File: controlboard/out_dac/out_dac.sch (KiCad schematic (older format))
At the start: 16 parts, among them J1 CONN_01X20, U1 PCM5102

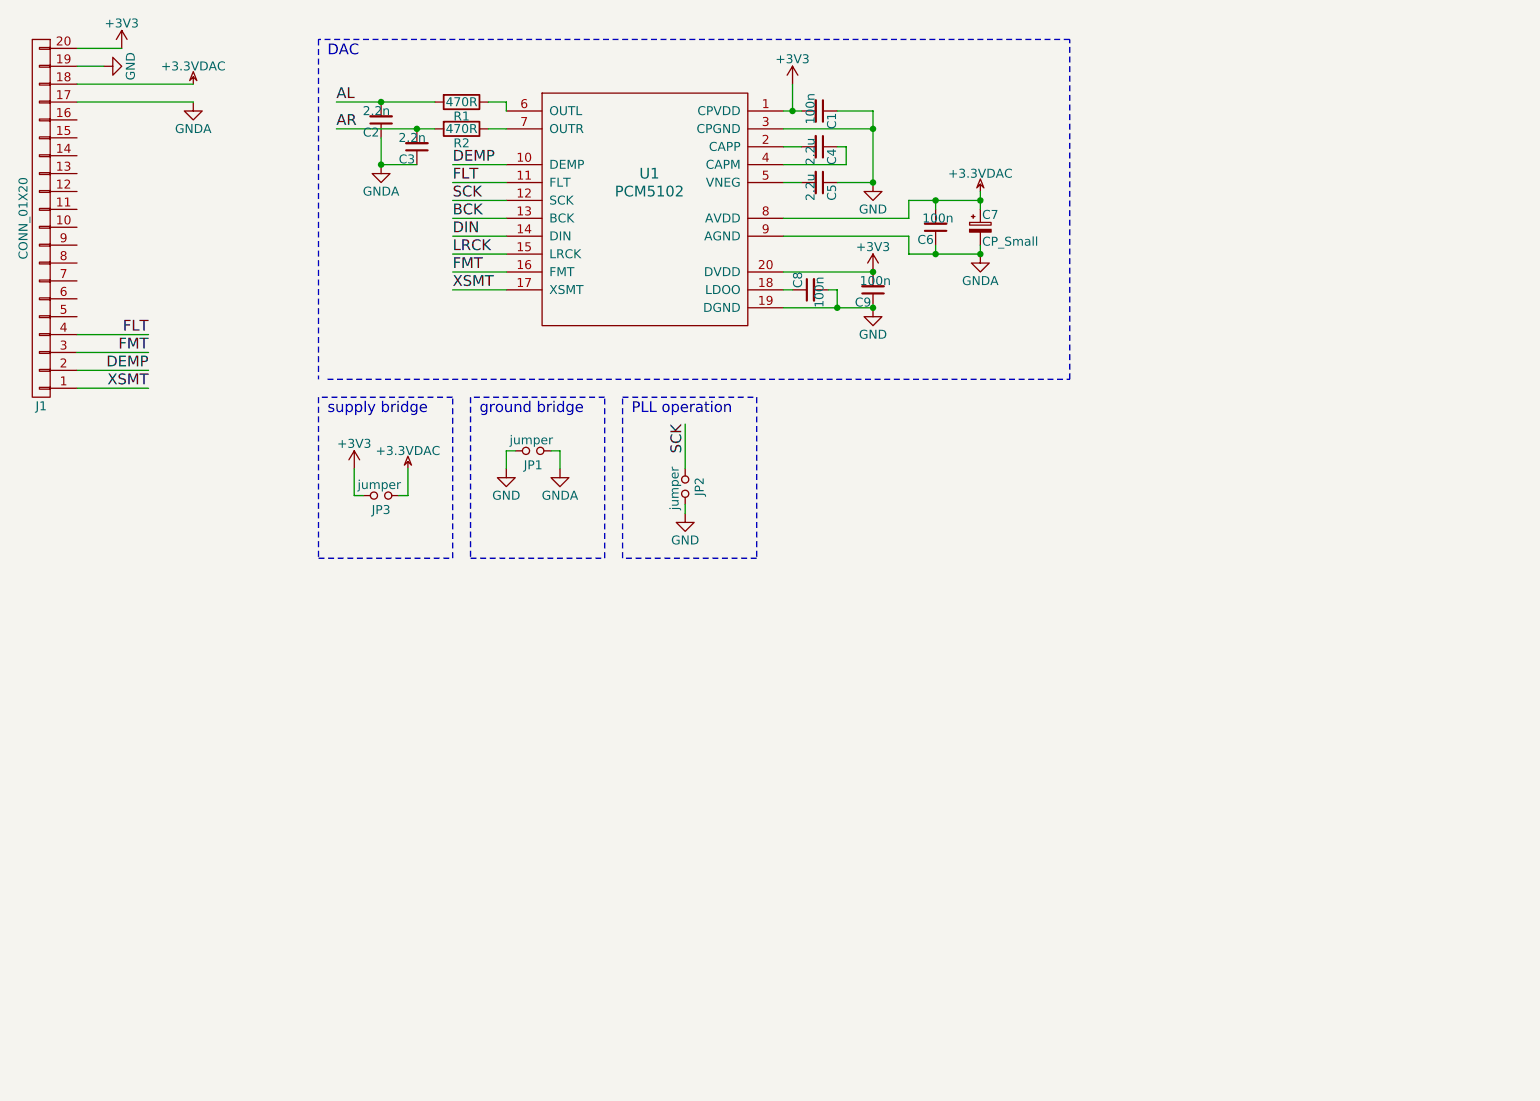
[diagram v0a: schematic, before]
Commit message: add vol control IC
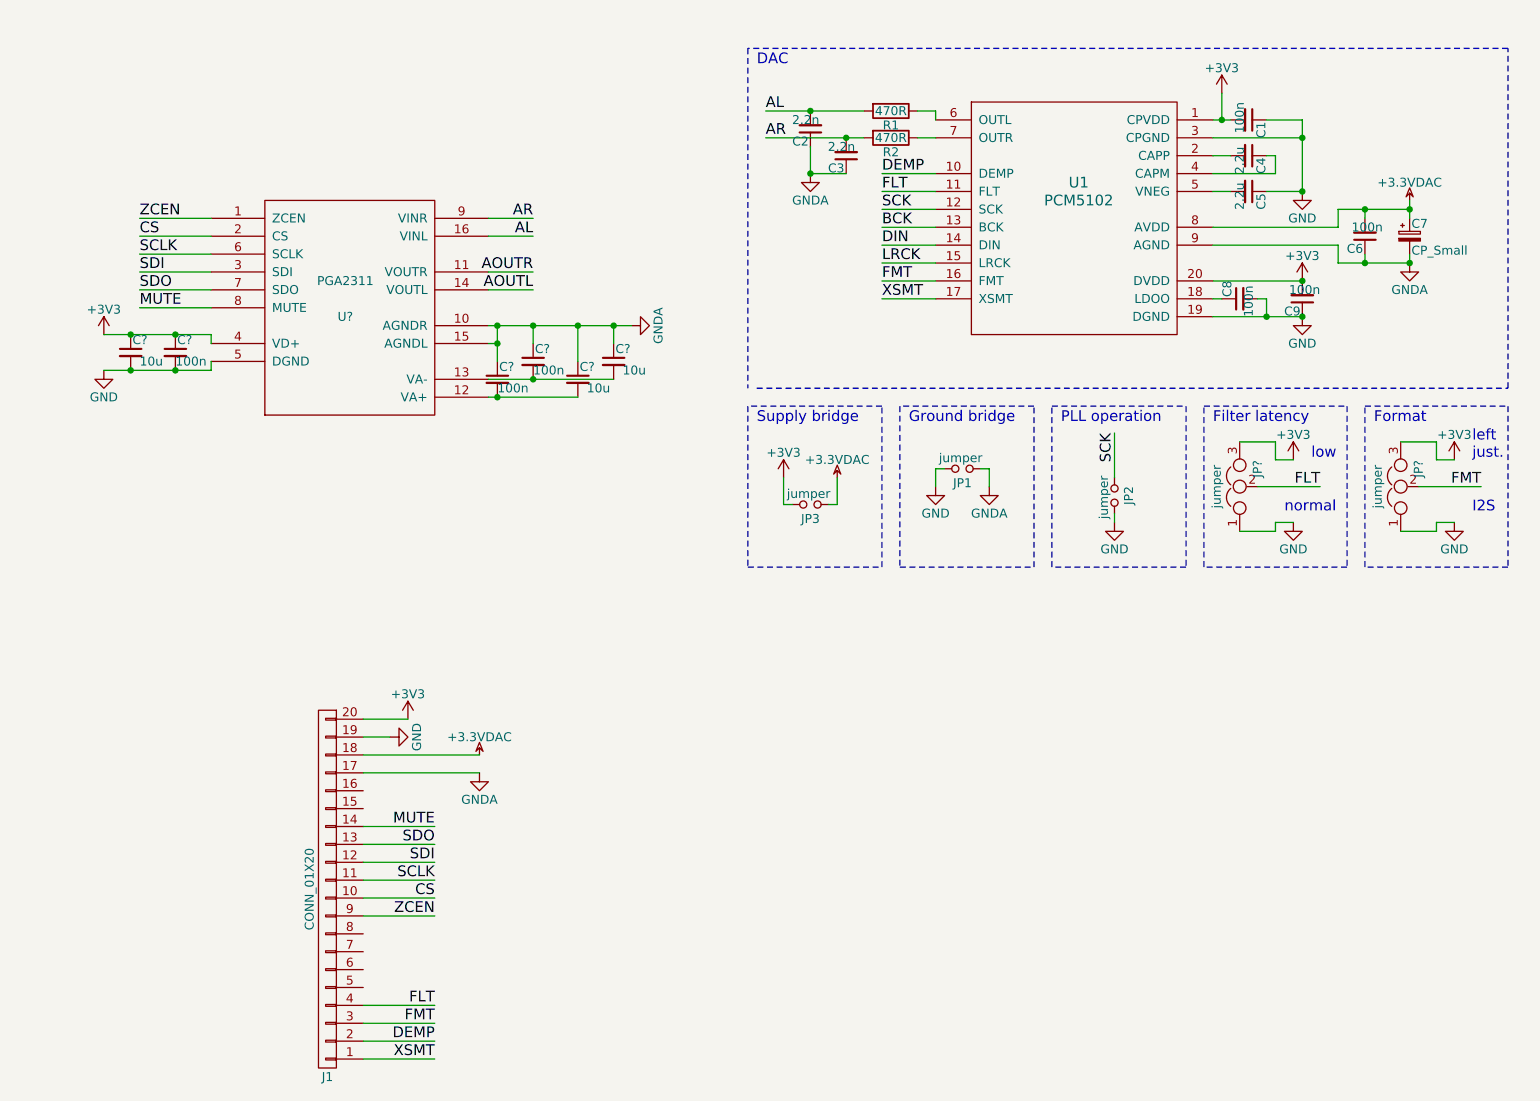
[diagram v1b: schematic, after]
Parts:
- added C? (x3): 100n, symbol C_Small
- added C? (x3): 10u, symbol C_Small
- added JP? (x2): jumper, symbol Jumper_NC_Dual
- added U?: PGA2311, symbol PGA2311
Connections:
- net +3V3: now also C?.1, C?.1, JP?.3, JP?.3, U?.4 (VD+)
- net AL: now also U?.16 (VINL)
- net AR: now also U?.9 (VINR)
- net FLT: now also JP?.2
- net FMT: now also JP?.2
- net GND: now also C?.2, C?.2, JP?.1, JP?.1, U?.5 (DGND)
- net GNDA: now also C?.1, C?.1, C?.1, C?.1, U?.10 (AGNDR), U?.15 (AGNDL)
- net CS: now reaches J1.10 (P10)
- net CS: now also U?.2 (CS)
- net SCLK: now reaches J1.11 (P11)
- net SCLK: now also U?.6 (SCLK)
- net SDI: now reaches J1.12 (P12)
- net SDI: now also U?.3 (SDI)
- net SDO: now reaches J1.13 (P13)
- net SDO: now also U?.7 (SDO)
- net MUTE: now reaches J1.14 (P14)
- net MUTE: now also U?.8 (MUTE)
- net ZCEN: now reaches J1.9 (P9)
- net ZCEN: now also U?.1 (ZCEN)
- new net: C?.2, C?.2, U?.12 (VA+)
- new net: C?.2, C?.2, U?.13 (VA-)
- new net AOUTL: U?.14 (VOUTL)
- new net AOUTR: U?.11 (VOUTR)
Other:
- note added: "Filter latency"
- note added: "Format"
- note added: "Ground bridge"
- note added: "I2S"
- note added: "Supply bridge"
- note added: "left\njust."
- note added: "low"
- note added: "normal"
- note removed: "ground bridge"
- note removed: "supply bridge"
- moved on the sheet: C1, C2, C3, C4, C5, C6, C7, C8, C9, J1, JP1, JP2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
